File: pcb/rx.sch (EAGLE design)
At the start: 8 parts, among them IC1 REG1117, IC2 STM32F042K6, J1 USB_A_PTH_MALE

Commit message: cleanup
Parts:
- removed IC1: REG1117, usbclogger:REG1117
- added IC3: REG1117, clock:REG1117
- added JP1: (no value), adafruit:PINHD-1X6CLEAN
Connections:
- net GND: now also IC3.GND; no longer IC1.GND
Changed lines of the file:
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@@
 <part name="E1" library="SparkFun-RF" deviceset="ANTENNA-GROUNDED" device="TRACE-15.2MM"/>
 <part name="U$1" library="3pos_slide_switch" deviceset="SW_3POS_DEV" device="SW_3POS_OFFICIAL"/>
-<part name="IC1" library="usbclogger" deviceset="REG1117" device=""/>
-<part name="GND2" library="clock" deviceset="GND" device=""/>
 <part name="S1" library="Adafruit Feather M0 Adalogger" deviceset="SWITCH-MOMENTARY-2" device="TURTLE"/>
 <part name="D1" library="nixx" deviceset="RGB_LED_CA" device="-150141M173100-R&amp;G&amp;B"/>
+<part name="IC3" library="clock" deviceset="REG1117" device=""/>
+<part name="GND7" library="supply1" library_urn="urn:adsk.eagle:library:371" deviceset="GND" device=""/>
+<part name="JP1" library="adafruit" deviceset="PINHD-1X6" device="CLEAN"/>
 </parts>
 <sheets>
@@
 <instance part="E1" gate="G$1" x="-20.32" y="43.18"/>
 <instance part="U$1" gate="G$1" x="-25.4" y="63.5"/>
-<instance part="IC1" gate="G$1" x="-30.48" y="2.54"/>
-<instance part="GND2" gate="1" x="-30.48" y="-12.7"/>
 <instance part="S1" gate="G$1" x="-53.34" y="25.4"/>
 <instance part="D1" gate="G$1" x="40.64" y="76.2"/>
+<instance part="IC3" gate="G$1" x="-30.48" y="-30.48"/>
+<instance part="GND7" gate="1" x="-30.48" y="-45.72"/>
+<instance part="JP1" gate="A" x="7.62" y="-2.54"/>
 </instances>
 <busses>
@@
 <net name="GND" class="0">
 <segment>
-<pinref part="IC1" gate="G$1" pin="GND"/>
-<pinref part="GND2" gate="1" pin="GND"/>
+<pinref part="IC3" gate="G$1" pin="GND"/>
+<pinref part="GND7" gate="1" pin="GND"/>
 </segment>
 </net>

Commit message: dt rx done
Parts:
- removed IC3: REG1117, clock:REG1117
- removed JP1: (no value), adafruit:PINHD-1X6CLEAN
- added C1, C12, C13, C3: 100nF, clock:CAP0805
- added C10, C11: 1uF, clock:CAP0805
- added C2, C6: 2.2nF, clock:CAP0805
- added C4: 1.5pF, clock:CAP0805
- added C5: 1pF, clock:CAP0805
- added C7: 4.7pF, clock:CAP0805
- added C8, C9: 22pF, clock:CAP0805
- added JP2: (no value), adafruit_changed:PINHD-1X8CLEANBIG
- added L1: 3.9nH, basicBoard:INDUCTOR0805
- added L2: 8.2nH, basicBoard:INDUCTOR0805
- added L3: 2.7nH, basicBoard:INDUCTOR0805
- added R1, R2, R3, R4, R5: 22K, joyAnalog:RESISTOR0805-RES
- added SJ1, SJ2, SJ3: JUMPER-SMT_2_NC_TRACE_NO-SILK, SparkFun-Jumpers:JUMPER-SMT_2_NC_TRACE_NO-SILK
- added U$4: XC6206_DEV, 3pos_slide_switch:XC6206_DEV
- added Y1: CRYSTAL-26MHZSMD-3.2X2.5, SparkFun-Clocks:CRYSTAL-26MHZSMD-3.2X2.5
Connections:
- new net +3V3: C1.1, C11.1, C12.1, C13.1, C2.1, D1.A, IC2.VDD, IC2.VDDA, JP2.5, S1.2, SJ1.1, SJ2.1, SJ3.1, U$3.VDD@15, U$3.VDD@18, U$3.VDD@7, U$4.OUT
- new net +5V: C10.1, J1.VBUS, JP2.7, U$4.IN
- new net N$1: C3.1, U$3.DVDD
- new net N$10: IC2.PA0, U$1.D
- new net N$11: IC2.PB8, R2.1, S1.1
- new net N$12: IC2.PA11, J1.D-
- new net N$13: IC2.PA12, J1.D+
- new net N$14: IC2.PB5, U$3.MOSI
- new net N$15: IC2.PB4, U$3.MISO
- new net N$16: IC2.PB3, U$3.SCK
- new net N$17: D1.GC, R3.1
- new net N$18: D1.RC, R4.1
- new net N$19: D1.BC, R5.1
- new net N$2: R1.1, U$3.IREF
- new net N$20: IC2.PF0/OSC_IN, U$3.CSN
- new net N$21: IC2.PF1/OSC_OUT, U$3.CE
- new net N$22: IC2.PA14/SWCLK, JP2.1
- new net N$23: IC2.PA13/SWDIO, JP2.2
- new net N$24: IC2.PA10, JP2.3
- new net N$25: IC2.PA9, JP2.4
- new net N$26: IC2.PA1, U$1.C
- new net N$27: IC2.PA2, U$1.B
- new net N$28: IC2.PA3, U$1.A
- new net N$29: IC2.PA15, R4.2
- new net N$3: L1.1, L2.1, U$3.ANT2
- new net N$30: IC2.PB6, R3.2
- new net N$31: IC2.PB7, R5.2
- new net N$32: IC2.PA4, SJ3.2
- new net N$33: IC2.PA6, SJ2.2
- new net N$34: IC2.PB0, SJ1.2
- new net N$4: C4.1, L1.2
- new net N$5: C4.2, C5.1, E1.SIGNAL
- new net N$6: L2.2, L3.1, U$3.ANT1
- new net N$7: C8.1, U$3.XC2, Y1.1
- new net N$8: C6.1, C7.1, L3.2, U$3.VDD_PA
- new net N$9: C9.1, U$3.XC1, Y1.2
- net GND: now also C1.2, C10.2, C11.2, C12.2, C13.2, C2.2, C3.2, C5.2, C6.2, C7.2, C8.2, C9.2, E1.GND, IC2.VSS, J1.GND, J1.SHIELD, JP2.6, R1.2, R2.2, U$1.GND, U$3.VSS@0, U$3.VSS@14, U$3.VSS@17, U$3.VSS@20, U$3.VSS@8, U$4.GND, Y1.3; no longer IC3.GND
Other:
- moved on the sheet: E1, IC2, J1, S1, U$3

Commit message: cleanup
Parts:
- C10, C11: value 1uF -> 4.7uF
- R2: value 22K -> 10K
- R3: value 22K -> 4.7K
- R4, R5: value 22K -> 2.2K
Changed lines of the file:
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@@
 <part name="GND13" library="supply1" library_urn="urn:adsk.eagle:library:371" deviceset="GND" device=""/>
 <part name="GND15" library="supply1" library_urn="urn:adsk.eagle:library:371" deviceset="GND" device=""/>
-<part name="C10" library="clock" deviceset="CAP" device="0805" value="1uF"/>
-<part name="C11" library="clock" deviceset="CAP" device="0805" value="1uF"/>
+<part name="C10" library="clock" deviceset="CAP" device="0805" value="4.7uF"/>
+<part name="C11" library="clock" deviceset="CAP" device="0805" value="4.7uF"/>
 <part name="GND16" library="supply1" library_urn="urn:adsk.eagle:library:371" deviceset="GND" device=""/>
 <part name="GND17" library="supply1" library_urn="urn:adsk.eagle:library:371" deviceset="GND" device=""/>
 <part name="Y1" library="SparkFun-Clocks" deviceset="CRYSTAL-26MHZ" device="SMD-3.2X2.5"/>
-<part name="R2" library="joyAnalog" deviceset="RESISTOR" device="0805-RES" value="22K"/>
+<part name="R2" library="joyAnalog" deviceset="RESISTOR" device="0805-RES" value="10K"/>
 <part name="GND9" library="supply1" library_urn="urn:adsk.eagle:library:371" deviceset="GND" device=""/>
 <part name="+3V2" library="supply1" library_urn="urn:adsk.eagle:library:371" deviceset="+3V3" device=""/>
@@
 <part name="GND19" library="supply1" library_urn="urn:adsk.eagle:library:371" deviceset="GND" device=""/>
 <part name="GND20" library="supply1" library_urn="urn:adsk.eagle:library:371" deviceset="GND" device=""/>
-<part name="R3" library="joyAnalog" deviceset="RESISTOR" device="0805-RES" value="22K"/>
-<part name="R4" library="joyAnalog" deviceset="RESISTOR" device="0805-RES" value="22K"/>
-<part name="R5" library="joyAnalog" deviceset="RESISTOR" device="0805-RES" value="22K"/>
+<part name="R3" library="joyAnalog" deviceset="RESISTOR" device="0805-RES" value="4.7K"/>
+<part name="R4" library="joyAnalog" deviceset="RESISTOR" device="0805-RES" value="2.2K"/>
+<part name="R5" library="joyAnalog" deviceset="RESISTOR" device="0805-RES" value="2.2K"/>
 <part name="+3V4" library="supply1" library_urn="urn:adsk.eagle:library:371" deviceset="+3V3" device=""/>
 <part name="JP2" library="adafruit_changed" deviceset="PINHD-1X8" device="CLEANBIG"/>

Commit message: further cleanup
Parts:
- removed D1: RGB_LED_CA-150141M173100-R&G&B, nixx:RGB_LED_CA-150141M173100-R&G&B
- removed R3: 4.7K, joyAnalog:RESISTOR0805-RES
- removed R5: 2.2K, joyAnalog:RESISTOR0805-RES
- removed S1: SWITCH-MOMENTARY-2TURTLE, Adafruit Feather M0 Adalogger:SWITCH-MOMENTARY-2TURTLE
- removed SJ3: JUMPER-SMT_2_NC_TRACE_NO-SILK, SparkFun-Jumpers:JUMPER-SMT_2_NC_TRACE_NO-SILK
- added LED2: (no value), joyAnalog:LEDCHIP-LED0805
- added U$10: 324_SW, 3pos_slide_switch:324_SW
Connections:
- removed net N$19: D1.BC, R5.1
- removed net N$30: IC2.PB6, R3.2
- removed net N$31: IC2.PB7, R5.2
- removed net N$32: IC2.PA4, SJ3.2
- net +3V3: now also U$10.1, U$10.4; no longer D1.A, S1.2, SJ3.1
- net GND: now also LED2.C
- net N$11: now also U$10.2, U$10.3; no longer S1.1
- net N$17: now also IC2.PB6, U$3.IRQ; no longer D1.GC, R3.1
- net N$18: now also LED2.A; no longer D1.RC
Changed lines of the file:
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@@
 <part name="E1" library="SparkFun-RF" deviceset="ANTENNA-GROUNDED" device="TRACE-15.2MM"/>
 <part name="U$1" library="3pos_slide_switch" deviceset="SW_3POS_DEV" device="SW_3POS_OFFICIAL"/>
-<part name="S1" library="Adafruit Feather M0 Adalogger" deviceset="SWITCH-MOMENTARY-2" device="TURTLE"/>
-<part name="D1" library="nixx" deviceset="RGB_LED_CA" device="-150141M173100-R&amp;G&amp;B"/>
 <part name="GND7" library="supply1" library_urn="urn:adsk.eagle:library:371" deviceset="GND" device=""/>
 <part name="+3V1" library="supply1" library_urn="urn:adsk.eagle:library:371" deviceset="+3V3" device=""/>
@@
 <part name="GND19" library="supply1" library_urn="urn:adsk.eagle:library:371" deviceset="GND" device=""/>
 <part name="GND20" library="supply1" library_urn="urn:adsk.eagle:library:371" deviceset="GND" device=""/>
-<part name="R3" library="joyAnalog" deviceset="RESISTOR" device="0805-RES" value="4.7K"/>
 <part name="R4" library="joyAnalog" deviceset="RESISTOR" device="0805-RES" value="2.2K"/>
-<part name="R5" library="joyAnalog" deviceset="RESISTOR" device="0805-RES" value="2.2K"/>
-<part name="+3V4" library="supply1" library_urn="urn:adsk.eagle:library:371" deviceset="+3V3" device=""/>
 <part name="JP2" library="adafruit_changed" deviceset="PINHD-1X8" device="CLEANBIG"/>
 <part name="+3V5" library="supply1" library_urn="urn:adsk.eagle:library:371" deviceset="+3V3" device=""/>
@@
 <part name="SJ1" library="SparkFun-Jumpers" deviceset="JUMPER-SMT_2_NC_TRACE" device="_NO-SILK"/>
 <part name="SJ2" library="SparkFun-Jumpers" deviceset="JUMPER-SMT_2_NC_TRACE" device="_NO-SILK"/>
-<part name="SJ3" library="SparkFun-Jumpers" deviceset="JUMPER-SMT_2_NC_TRACE" device="_NO-SILK"/>
 <part name="+3V6" library="supply1" library_urn="urn:adsk.eagle:library:371" deviceset="+3V3" device=""/>
 <part name="+3V7" library="supply1" library_urn="urn:adsk.eagle:library:371" deviceset="+3V3" device=""/>
-<part name="+3V8" library="supply1" library_urn="urn:adsk.eagle:library:371" deviceset="+3V3" device=""/>
+<part name="U$10" library="3pos_slide_switch" deviceset="324_SW" device=""/>
+<part name="LED2" library="joyAnalog" deviceset="LED" device="CHIP-LED0805"/>
+<part name="GND22" library="supply1" library_urn="urn:adsk.eagle:library:371" deviceset="GND" device=""/>
 </parts>
 <sheets>
@@
 <instance part="E1" gate="G$1" x="294.64" y="-38.1" rot="R270"/>
 <instance part="U$1" gate="G$1" x="106.68" y="15.24" rot="R90"/>
-<instance part="S1" gate="G$1" x="86.36" y="-50.8"/>
-<instance part="D1" gate="G$1" x="40.64" y="76.2"/>
 <instance part="GND7" gate="1" x="-30.48" y="-48.26"/>
 <instance part="+3V1" gate="G$1" x="170.18" y="2.54"/>
@@
 <instance part="R2" gate="G$1" x="76.2" y="-55.88" rot="R270"/>
 <instance part="GND9" gate="1" x="76.2" y="-63.5"/>
-<instance part="+3V2" gate="G$1" x="96.52" y="-48.26"/>
+<instance part="+3V2" gate="G$1" x="121.92" y="-55.88"/>
 <instance part="+3V3" gate="G$1" x="22.86" y="15.24"/>
 <instance part="GND18" gate="1" x="22.86" y="-53.34"/>
@@
 <instance part="GND19" gate="1" x="-5.08" y="-38.1"/>
 <instance part="GND20" gate="1" x="2.54" y="-38.1"/>
-<instance part="R3" gate="G$1" x="55.88" y="83.82"/>
 <instance part="R4" gate="G$1" x="55.88" y="76.2"/>
-<instance part="R5" gate="G$1" x="55.88" y="68.58"/>
-<instance part="+3V4" gate="G$1" x="22.86" y="78.74"/>
 <instance part="JP2" gate="G$1" x="119.38" y="-17.78"/>
 <instance part="+3V5" gate="G$1" x="127" y="-17.78"/>
@@
 <instance part="SJ1" gate="G$1" x="53.34" y="40.64"/>
 <instance part="SJ2" gate="G$1" x="53.34" y="33.02"/>
-<instance part="SJ3" gate="G$1" x="53.34" y="25.4"/>
 <instance part="+3V6" gate="G$1" x="43.18" y="43.18"/>
 <instance part="+3V7" gate="G$1" x="43.18" y="35.56"/>
-<instance part="+3V8" gate="G$1" x="43.18" y="27.94"/>
+<instance part="U$10" gate="G$1" x="96.52" y="-55.88"/>
+<instance part="LED2" gate="G$1" x="43.18" y="76.2" rot="R270"/>
+<instance part="GND22" gate="1" x="33.02" y="73.66"/>
 </instances>
 <busses>
@@
 <wire x1="106.68" y1="-22.86" x2="116.84" y2="-22.86" width="0.1524" layer="91"/>
 </segment>
+<segment>
+<pinref part="GND22" gate="1" pin="GND"/>
+<pinref part="LED2" gate="G$1" pin="C"/>
+<wire x1="33.02" y1="76.2" x2="38.1" y2="76.2" width="0.1524" layer="91"/>
+</segment>
 </net>
 <net name="+3V3" class="0">
@@
 </segment>
 <segment>
-<pinref part="S1" gate="G$1" pin="2"/>
-<pinref part="+3V2" gate="G$1" pin="+3V3"/>
-<wire x1="91.44" y1="-50.8" x2="96.52" y2="-50.8" width="0.1524" layer="91"/>
-</segment>
-<segment>
 <pinref part="+3V3" gate="G$1" pin="+3V3"/>
 <pinref part="IC2" gate="G$1" pin="VDD"/>
@@
 </segment>
 <segment>
-<pinref part="D1" gate="G$1" pin="A"/>
-<pinref part="+3V4" gate="G$1" pin="+3V3"/>
-<wire x1="30.48" y1="76.2" x2="22.86" y2="76.2" width="0.1524" layer="91"/>
-</segment>
-<segment>
 <pinref part="JP2" gate="G$1" pin="5"/>
 <pinref part="+3V5" gate="G$1" pin="+3V3"/>
@@
 </segment>
 <segment>
-<pinref part="+3V8" gate="G$1" pin="+3V3"/>
-<pinref part="SJ3" gate="G$1" pin="1"/>
-<wire x1="43.18" y1="25.4" x2="48.26" y2="25.4" width="0.1524" layer="91"/>
+<pinref part="U$10" gate="G$1" pin="4"/>
+<pinref part="+3V2" gate="G$1" pin="+3V3"/>
+<wire x1="111.76" y1="-58.42" x2="121.92" y2="-58.42" width="0.1524" layer="91"/>
+<pinref part="U$10" gate="G$1" pin="1"/>
+<wire x1="111.76" y1="-58.42" x2="81.28" y2="-58.42" width="0.1524" layer="91"/>
+<junction x="111.76" y="-58.42"/>
 </segment>
 </net>
@@
 <segment>
 <pinref part="IC2" gate="G$1" pin="PB8"/>
-<pinref part="S1" gate="G$1" pin="1"/>
 <wire x1="71.12" y1="-50.8" x2="76.2" y2="-50.8" width="0.1524" layer="91"/>
 <pinref part="R2" gate="G$1" pin="1"/>
+<pinref part="U$10" gate="G$1" pin="2"/>
 <wire x1="76.2" y1="-50.8" x2="81.28" y2="-50.8" width="0.1524" layer="91"/>
 <junction x="76.2" y="-50.8"/>
+<pinref part="U$10" gate="G$1" pin="3"/>
+<wire x1="81.28" y1="-50.8" x2="111.76" y2="-50.8" width="0.1524" layer="91"/>
+<junction x="81.28" y="-50.8"/>
 </segment>
 </net>
@@
 </segment>
 </net>
-<net name="N$17" class="0">
-<segment>
-<pinref part="D1" gate="G$1" pin="GC"/>
-<pinref part="R3" gate="G$1" pin="1"/>
-<wire x1="45.72" y1="83.82" x2="50.8" y2="83.82" width="0.1524" layer="91"/>
-</segment>
-</net>
 <net name="N$18" class="0">
 <segment>
-<pinref part="D1" gate="G$1" pin="RC"/>
 <pinref part="R4" gate="G$1" pin="1"/>
 <wire x1="45.72" y1="76.2" x2="50.8" y2="76.2" width="0.1524" layer="91"/>
-</segment>
-</net>
-<net name="N$19" class="0">
-<segment>
-<pinref part="D1" gate="G$1" pin="BC"/>
-<pinref part="R5" gate="G$1" pin="1"/>
-<wire x1="45.72" y1="68.58" x2="50.8" y2="68.58" width="0.1524" layer="91"/>
+<pinref part="LED2" gate="G$1" pin="A"/>
 </segment>
 </net>
@@
 </segment>
 </net>
-<net name="N$30" class="0">
-<segment>
-<pinref part="IC2" gate="G$1" pin="PB6"/>
-<wire x1="71.12" y1="-45.72" x2="86.36" y2="-45.72" width="0.1524" layer="91"/>
-<wire x1="86.36" y1="-45.72" x2="86.36" y2="43.18" width="0.1524" layer="91"/>
-<pinref part="R3" gate="G$1" pin="2"/>
-<wire x1="86.36" y1="43.18" x2="86.36" y2="83.82" width="0.1524" layer="91"/>
-<wire x1="86.36" y1="83.82" x2="60.96" y2="83.82" width="0.1524" layer="91"/>
-</segment>
-</net>
-<net name="N$31" class="0">
-<segment>
-<pinref part="IC2" gate="G$1" pin="PB7"/>
-<wire x1="71.12" y1="-48.26" x2="83.82" y2="-48.26" width="0.1524" layer="91"/>
-<wire x1="83.82" y1="-48.26" x2="83.82" y2="68.58" width="0.1524" layer="91"/>
-<pinref part="R5" gate="G$1" pin="2"/>
-<wire x1="83.82" y1="68.58" x2="60.96" y2="68.58" width="0.1524" layer="91"/>
-</segment>
-</net>
-<net name="N$32" class="0">
-<segment>
-<pinref part="IC2" gate="G$1" pin="PA4"/>
-<pinref part="SJ3" gate="G$1" pin="2"/>
-<wire x1="71.12" y1="2.54" x2="58.42" y2="2.54" width="0.1524" layer="91"/>
-<wire x1="58.42" y1="2.54" x2="58.42" y2="25.4" width="0.1524" layer="91"/>
-</segment>
-</net>
 <net name="N$33" class="0">
 <segment>
@@
 </segment>
 </net>
+<net name="N$17" class="0">
+<segment>
+<pinref part="IC2" gate="G$1" pin="PB6"/>
+<wire x1="71.12" y1="-45.72" x2="121.92" y2="-45.72" width="0.1524" layer="91"/>
+<wire x1="121.92" y1="-45.72" x2="121.92" y2="-48.26" width="0.1524" layer="91"/>
+<pinref part="U$3" gate="G$1" pin="IRQ"/>
+<wire x1="121.92" y1="-48.26" x2="149.86" y2="-48.26" width="0.1524" layer="91"/>
+</segment>
+</net>

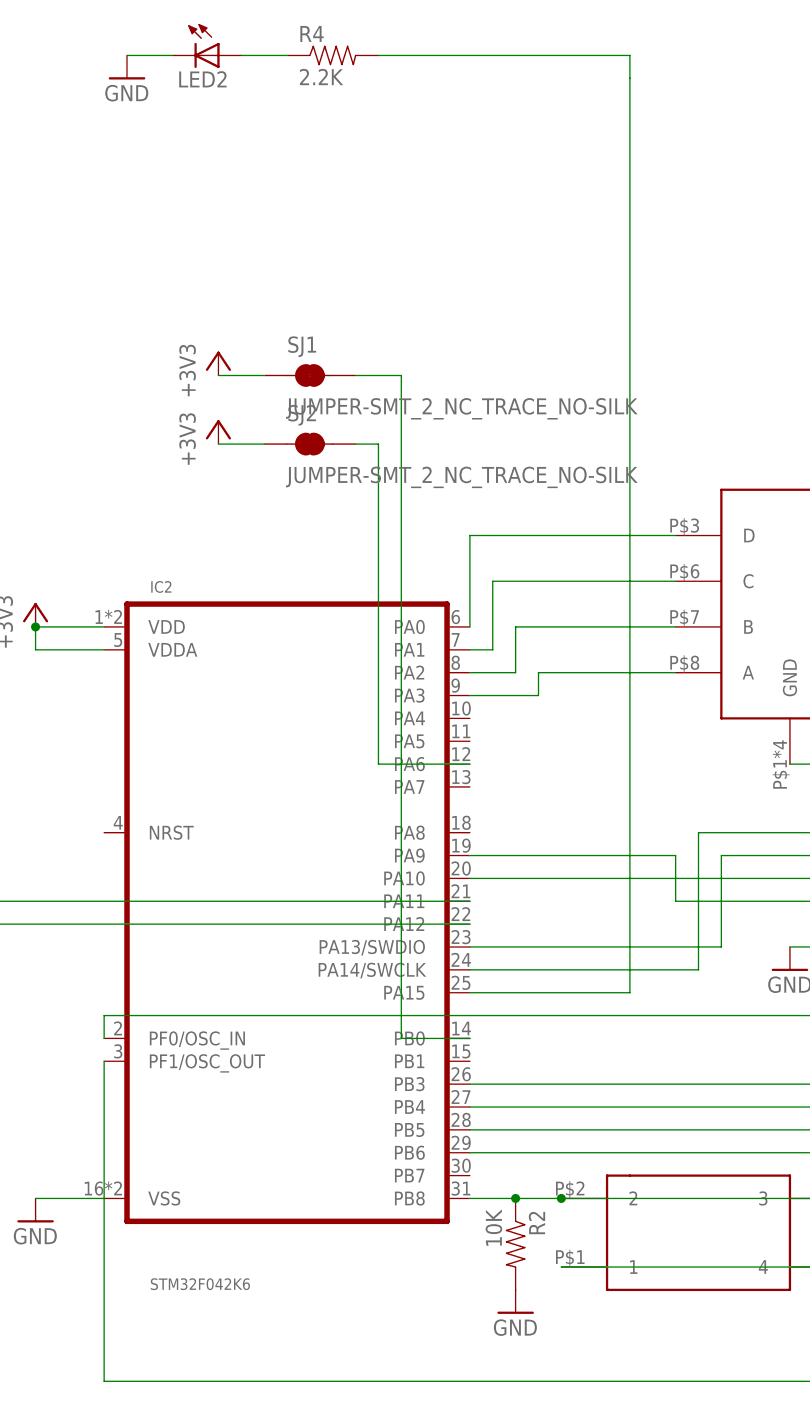
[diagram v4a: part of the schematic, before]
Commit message: thinking about switch to tssop20
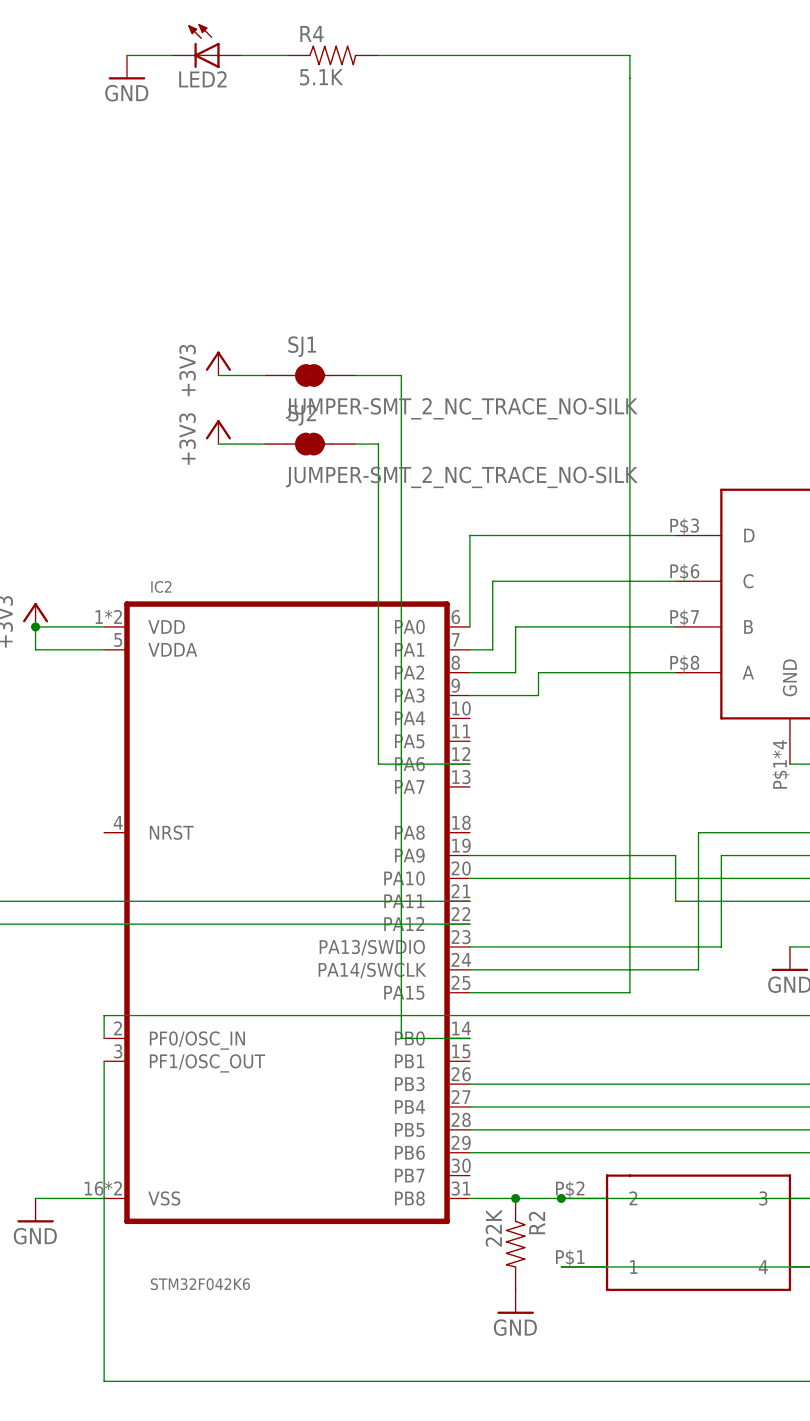
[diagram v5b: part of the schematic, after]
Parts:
- R2: value 10K -> 22K
- R4: value 2.2K -> 5.1K
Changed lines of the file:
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@@
 <part name="GND17" library="supply1" library_urn="urn:adsk.eagle:library:371" deviceset="GND" device=""/>
 <part name="Y1" library="SparkFun-Clocks" deviceset="CRYSTAL-26MHZ" device="SMD-3.2X2.5"/>
-<part name="R2" library="joyAnalog" deviceset="RESISTOR" device="0805-RES" value="10K"/>
+<part name="R2" library="joyAnalog" deviceset="RESISTOR" device="0805-RES" value="22K"/>
 <part name="GND9" library="supply1" library_urn="urn:adsk.eagle:library:371" deviceset="GND" device=""/>
 <part name="+3V2" library="supply1" library_urn="urn:adsk.eagle:library:371" deviceset="+3V3" device=""/>
@@
 <part name="GND19" library="supply1" library_urn="urn:adsk.eagle:library:371" deviceset="GND" device=""/>
 <part name="GND20" library="supply1" library_urn="urn:adsk.eagle:library:371" deviceset="GND" device=""/>
-<part name="R4" library="joyAnalog" deviceset="RESISTOR" device="0805-RES" value="2.2K"/>
+<part name="R4" library="joyAnalog" deviceset="RESISTOR" device="0805-RES" value="5.1K"/>
 <part name="JP2" library="adafruit_changed" deviceset="PINHD-1X8" device="CLEANBIG"/>
 <part name="+3V5" library="supply1" library_urn="urn:adsk.eagle:library:371" deviceset="+3V3" device=""/>
